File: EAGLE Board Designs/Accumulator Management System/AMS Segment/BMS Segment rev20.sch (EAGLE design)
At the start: 161 parts, among them J1 CONNECTOR-2_MICROFIT_SMD_RIGH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, J10 CONNECTOR-2_MICROFIT_SMD_RIGH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, J100 CONNECTOR-1_5222_, J101 CONNECTOR-1_5222_, J102 CONNECTOR-1_5222_, J103 CONNECTOR-1_5222_, J104 CONNECTOR-1_5222_, J105 CONNECTOR-1_5222_, J106 CONNECTOR-1_5222_, J107 CONNECTOR-1_5222_, J108 CONNECTOR-1_5222_, J109 CONNECTOR-1_5222_, J11 CONNECTOR-2_MICROFIT_SMD_RIGH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, J110 CONNECTOR-1_5222_, J111 CONNECTOR-1_5222_, J112 CONNECTOR-1_5222_, J113 CONNECTOR-1_5222_, J114 CONNECTOR-1_5222_, J115 CONNECTOR-1_5222_, J116 CONNECTOR-1_5222_, J117 CONNECTOR-1_5222_, J118 CONNECTOR-1_5222_, J119 CONNECTOR-1_5222_, J12 CONNECTOR-2_MICROFIT_SMD_RIGH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, J120 CONNECTOR-1_5222_, J121 CONNECTOR-1_5222_, J2 CONNECTOR-2_MICROFIT_SMD_RIGH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, J3 CONNECTOR-2_MICROFIT_SMD_RIGH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, J4 CONNECTOR-2_MICROFIT_SMD_RIGH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, J6 CONNECTOR-2_MICROFIT_SMD_RIGH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, J8 CONNECTOR-2_MICROFIT_SMD_RIGH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, J9 CONNECTOR-2_MICROFIT_SMD_RIGH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, T2 TRANSFORMER_HM2112ZNLT, U1 SHT31-ARP-B, U2 LTC6811-1, U3 LT3990-5, U4 LT3990-5, U5 LTC6811-1, U6 SHT31-ARP-B

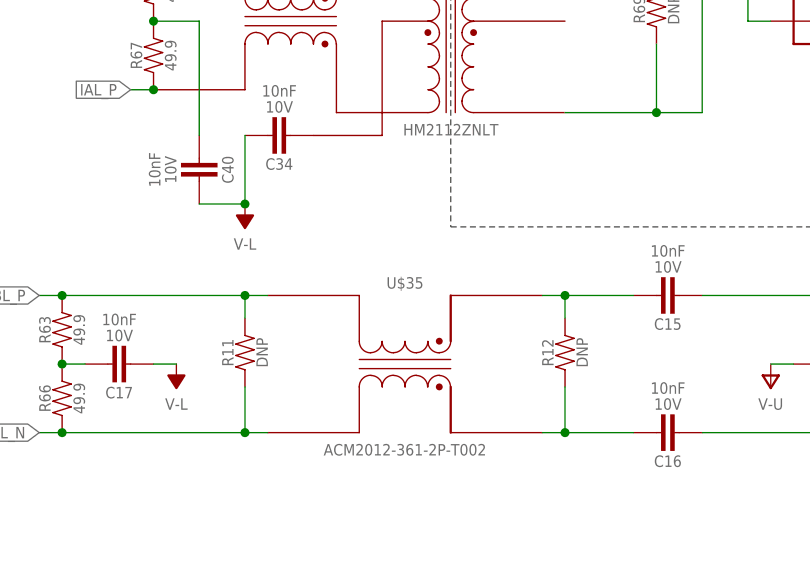
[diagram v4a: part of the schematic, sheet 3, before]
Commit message: Updates to Board
Added updates to board design.
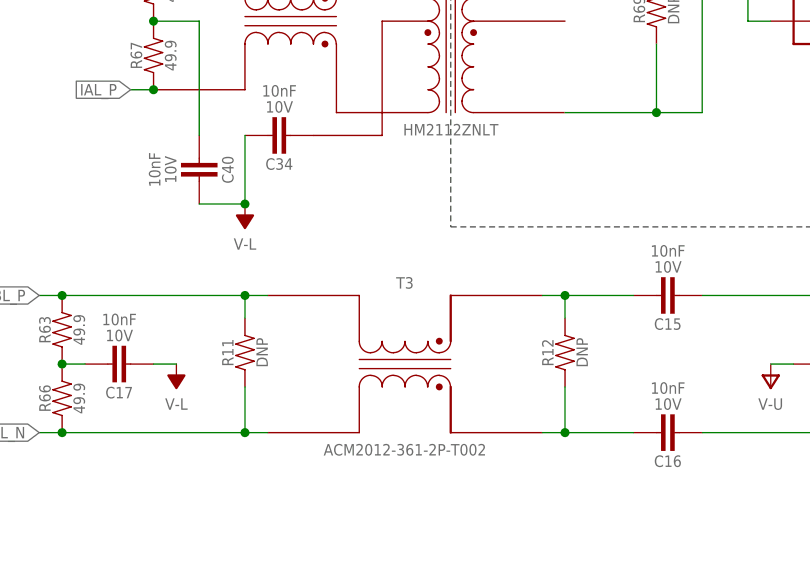
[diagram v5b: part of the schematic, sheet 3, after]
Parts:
- renumbered U$35 to T3
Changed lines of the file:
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@@
 <part name="P100" library="HyTechSupplies" deviceset="V-U" device=""/>
 <part name="R69" library="HyTechDevices" deviceset="RESISTOR_?_*" device="0603" technology="DNP" value="RESISTOR_0603_DNP"/>
-<part name="U$35" library="HyTechDevices" deviceset="ACM2012-361-2P-T002" device=""/>
+<part name="T3" library="HyTechDevices" deviceset="ACM2012-361-2P-T002" device=""/>
 <part name="U5" library="HyTechDevices" deviceset="LTC6811-1" device=""/>
 <part name="U2" library="HyTechDevices" deviceset="LTC6811-1" device=""/>
@@
 <attribute name="RESISTANCE" x="128.27" y="118.11" size="1.27" layer="96" rot="R90" align="top-center"/>
 </instance>
-<instance part="U$35" gate="G$1" x="99.06" y="78.74" smashed="yes">
+<instance part="T3" gate="G$1" x="99.06" y="78.74" smashed="yes">
 <attribute name="NAME" x="99.06" y="87.122" size="1.27" layer="95" align="bottom-center"/>
 <attribute name="MPN" x="99.06" y="69.85" size="1.27" layer="96" align="top-center"/>
@@
 <label x="58.42" y="71.12" size="1.27" layer="95" rot="R180" xref="yes"/>
 <pinref part="R66" gate="G$1" pin="1"/>
-<pinref part="U$35" gate="G$1" pin="2"/>
+<pinref part="T3" gate="G$1" pin="2"/>
 <wire x1="83.82" y1="71.12" x2="81.28" y2="71.12" width="0.1524" layer="91"/>
 <junction x="60.96" y="71.12"/>
@@
 <label x="58.42" y="86.36" size="1.27" layer="95" rot="R180" xref="yes"/>
 <pinref part="R63" gate="G$1" pin="2"/>
-<pinref part="U$35" gate="G$1" pin="1"/>
+<pinref part="T3" gate="G$1" pin="1"/>
 <wire x1="83.82" y1="86.36" x2="81.28" y2="86.36" width="0.1524" layer="91"/>
 <junction x="60.96" y="86.36"/>
@@
 <wire x1="124.46" y1="86.36" x2="116.84" y2="86.36" width="0.1524" layer="91"/>
 <wire x1="116.84" y1="86.36" x2="116.84" y2="83.82" width="0.1524" layer="91"/>
-<pinref part="U$35" gate="G$1" pin="4"/>
+<pinref part="T3" gate="G$1" pin="4"/>
 <wire x1="116.84" y1="86.36" x2="114.3" y2="86.36" width="0.1524" layer="91"/>
 <junction x="116.84" y="86.36"/>
@@
 <wire x1="124.46" y1="71.12" x2="116.84" y2="71.12" width="0.1524" layer="91"/>
 <wire x1="116.84" y1="71.12" x2="116.84" y2="76.2" width="0.1524" layer="91"/>
-<pinref part="U$35" gate="G$1" pin="3"/>
+<pinref part="T3" gate="G$1" pin="3"/>
 <wire x1="116.84" y1="71.12" x2="114.3" y2="71.12" width="0.1524" layer="91"/>
 <junction x="116.84" y="71.12"/>

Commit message: Added New Fuse Component
Changed fuses to cheaper, smaller package fuse components -- handles 3A, 125VDC.
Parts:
- F1, F10, F11, F12, F13, F14, F15, F16, F17, F18, F19, F2, F20, F21, F22, F23, F3, F4, F5, F6, F7, F8, F9: value FUSE_0885_1 -> FUSE__; device HyTechDevices:FUSE_0885_1 -> HyTechDevices:FUSE__2-SMD_3A
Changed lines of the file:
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@@
 <part name="P-4" library="HyTechSupplies" deviceset="V-L" device=""/>
 <part name="P+1" library="HyTechSupplies" deviceset="V+U" device=""/>
-<part name="F1" library="HyTechDevices" deviceset="FUSE_?_*" device="0885" technology="1" value="FUSE_0885_1"/>
-<part name="F4" library="HyTechDevices" deviceset="FUSE_?_*" device="0885" technology="1" value="FUSE_0885_1"/>
-<part name="F2" library="HyTechDevices" deviceset="FUSE_?_*" device="0885" technology="1" value="FUSE_0885_1"/>
-<part name="F5" library="HyTechDevices" deviceset="FUSE_?_*" device="0885" technology="1" value="FUSE_0885_1"/>
-<part name="F3" library="HyTechDevices" deviceset="FUSE_?_*" device="0885" technology="1" value="FUSE_0885_1"/>
-<part name="F9" library="HyTechDevices" deviceset="FUSE_?_*" device="0885" technology="1" value="FUSE_0885_1"/>
-<part name="F6" library="HyTechDevices" deviceset="FUSE_?_*" device="0885" technology="1" value="FUSE_0885_1"/>
-<part name="F10" library="HyTechDevices" deviceset="FUSE_?_*" device="0885" technology="1" value="FUSE_0885_1"/>
-<part name="F7" library="HyTechDevices" deviceset="FUSE_?_*" device="0885" technology="1" value="FUSE_0885_1"/>
-<part name="F11" library="HyTechDevices" deviceset="FUSE_?_*" device="0885" technology="1" value="FUSE_0885_1"/>
-<part name="F8" library="HyTechDevices" deviceset="FUSE_?_*" device="0885" technology="1" value="FUSE_0885_1"/>
-<part name="F13" library="HyTechDevices" deviceset="FUSE_?_*" device="0885" technology="1" value="FUSE_0885_1"/>
-<part name="F15" library="HyTechDevices" deviceset="FUSE_?_*" device="0885" technology="1" value="FUSE_0885_1"/>
-<part name="F14" library="HyTechDevices" deviceset="FUSE_?_*" device="0885" technology="1" value="FUSE_0885_1"/>
-<part name="F17" library="HyTechDevices" deviceset="FUSE_?_*" device="0885" technology="1" value="FUSE_0885_1"/>
-<part name="F16" library="HyTechDevices" deviceset="FUSE_?_*" device="0885" technology="1" value="FUSE_0885_1"/>
-<part name="F19" library="HyTechDevices" deviceset="FUSE_?_*" device="0885" technology="1" value="FUSE_0885_1"/>
-<part name="F18" library="HyTechDevices" deviceset="FUSE_?_*" device="0885" technology="1" value="FUSE_0885_1"/>
-<part name="F21" library="HyTechDevices" deviceset="FUSE_?_*" device="0885" technology="1" value="FUSE_0885_1"/>
+<part name="F1" library="HyTechDevices" deviceset="FUSE_?_*" device="" technology="2-SMD_3A" value="FUSE__"/>
+<part name="F4" library="HyTechDevices" deviceset="FUSE_?_*" device="" technology="2-SMD_3A" value="FUSE__"/>
+<part name="F2" library="HyTechDevices" deviceset="FUSE_?_*" device="" technology="2-SMD_3A" value="FUSE__"/>
+<part name="F5" library="HyTechDevices" deviceset="FUSE_?_*" device="" technology="2-SMD_3A" value="FUSE__"/>
+<part name="F3" library="HyTechDevices" deviceset="FUSE_?_*" device="" technology="2-SMD_3A" value="FUSE__"/>
+<part name="F9" library="HyTechDevices" deviceset="FUSE_?_*" device="" technology="2-SMD_3A" value="FUSE__"/>
+<part name="F6" library="HyTechDevices" deviceset="FUSE_?_*" device="" technology="2-SMD_3A" value="FUSE__"/>
+<part name="F10" library="HyTechDevices" deviceset="FUSE_?_*" device="" technology="2-SMD_3A" value="FUSE__"/>
+<part name="F7" library="HyTechDevices" deviceset="FUSE_?_*" device="" technology="2-SMD_3A" value="FUSE__"/>
+<part name="F11" library="HyTechDevices" deviceset="FUSE_?_*" device="" technology="2-SMD_3A" value="FUSE__"/>
+<part name="F8" library="HyTechDevices" deviceset="FUSE_?_*" device="" technology="2-SMD_3A" value="FUSE__"/>
+<part name="F13" library="HyTechDevices" deviceset="FUSE_?_*" device="" technology="2-SMD_3A" value="FUSE__"/>
+<part name="F15" library="HyTechDevices" deviceset="FUSE_?_*" device="" technology="2-SMD_3A" value="FUSE__"/>
+<part name="F14" library="HyTechDevices" deviceset="FUSE_?_*" device="" technology="2-SMD_3A" value="FUSE__"/>
+<part name="F17" library="HyTechDevices" deviceset="FUSE_?_*" device="" technology="2-SMD_3A" value="FUSE__"/>
+<part name="F16" library="HyTechDevices" deviceset="FUSE_?_*" device="" technology="2-SMD_3A" value="FUSE__"/>
+<part name="F19" library="HyTechDevices" deviceset="FUSE_?_*" device="" technology="2-SMD_3A" value="FUSE__"/>
+<part name="F18" library="HyTechDevices" deviceset="FUSE_?_*" device="" technology="2-SMD_3A" value="FUSE__"/>
+<part name="F21" library="HyTechDevices" deviceset="FUSE_?_*" device="" technology="2-SMD_3A" value="FUSE__"/>
 <part name="J101" library="HyTechDevices" deviceset="CONNECTOR-1_?_*" device="5222"/>
 <part name="J100" library="HyTechDevices" deviceset="CONNECTOR-1_?_*" device="5222"/>
@@
 <part name="J120" library="HyTechDevices" deviceset="CONNECTOR-1_?_*" device="5222"/>
 <part name="J121" library="HyTechDevices" deviceset="CONNECTOR-1_?_*" device="5222"/>
-<part name="F20" library="HyTechDevices" deviceset="FUSE_?_*" device="0885" technology="1" value="FUSE_0885_1"/>
-<part name="F22" library="HyTechDevices" deviceset="FUSE_?_*" device="0885" technology="1" value="FUSE_0885_1"/>
-<part name="F23" library="HyTechDevices" deviceset="FUSE_?_*" device="0885" technology="1" value="FUSE_0885_1"/>
+<part name="F20" library="HyTechDevices" deviceset="FUSE_?_*" device="" technology="2-SMD_3A" value="FUSE__"/>
+<part name="F22" library="HyTechDevices" deviceset="FUSE_?_*" device="" technology="2-SMD_3A" value="FUSE__"/>
+<part name="F23" library="HyTechDevices" deviceset="FUSE_?_*" device="" technology="2-SMD_3A" value="FUSE__"/>
 <part name="P26" library="HyTechSupplies" deviceset="V-U" device=""/>
 <part name="P28" library="HyTechSupplies" deviceset="V-U" device=""/>
@@
 <part name="P65" library="HyTechSupplies" deviceset="VREGU" device=""/>
 <part name="P66" library="HyTechSupplies" deviceset="VREGU" device=""/>
-<part name="F12" library="HyTechDevices" deviceset="FUSE_?_*" device="0885" technology="1" value="FUSE_0885_1"/>
+<part name="F12" library="HyTechDevices" deviceset="FUSE_?_*" device="" technology="2-SMD_3A" value="FUSE__"/>
 <part name="TP9" library="HyTechDevices" deviceset="TEST_POINT" device=""/>
 <part name="TP8" library="HyTechDevices" deviceset="TEST_POINT" device=""/>

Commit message: BMS Segment Universal Fuse, Buck
Fixed Buck routing and changed fuse footprint to universal footprint.
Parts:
- F1, F10, F11, F12, F13, F14, F15, F16, F17, F18, F19, F2, F20, F21, F22, F23, F3, F4, F5, F6, F7, F8, F9: device HyTechDevices:FUSE__2-SMD_3A -> HyTechDevices:FUSE_BMS-UNIVERSAL_
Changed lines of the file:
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@@
 <part name="P-4" library="HyTechSupplies" deviceset="V-L" device=""/>
 <part name="P+1" library="HyTechSupplies" deviceset="V+U" device=""/>
-<part name="F1" library="HyTechDevices" deviceset="FUSE_?_*" device="" technology="2-SMD_3A" value="FUSE__"/>
-<part name="F4" library="HyTechDevices" deviceset="FUSE_?_*" device="" technology="2-SMD_3A" value="FUSE__"/>
-<part name="F2" library="HyTechDevices" deviceset="FUSE_?_*" device="" technology="2-SMD_3A" value="FUSE__"/>
-<part name="F5" library="HyTechDevices" deviceset="FUSE_?_*" device="" technology="2-SMD_3A" value="FUSE__"/>
-<part name="F3" library="HyTechDevices" deviceset="FUSE_?_*" device="" technology="2-SMD_3A" value="FUSE__"/>
-<part name="F9" library="HyTechDevices" deviceset="FUSE_?_*" device="" technology="2-SMD_3A" value="FUSE__"/>
-<part name="F6" library="HyTechDevices" deviceset="FUSE_?_*" device="" technology="2-SMD_3A" value="FUSE__"/>
-<part name="F10" library="HyTechDevices" deviceset="FUSE_?_*" device="" technology="2-SMD_3A" value="FUSE__"/>
-<part name="F7" library="HyTechDevices" deviceset="FUSE_?_*" device="" technology="2-SMD_3A" value="FUSE__"/>
-<part name="F11" library="HyTechDevices" deviceset="FUSE_?_*" device="" technology="2-SMD_3A" value="FUSE__"/>
-<part name="F8" library="HyTechDevices" deviceset="FUSE_?_*" device="" technology="2-SMD_3A" value="FUSE__"/>
-<part name="F13" library="HyTechDevices" deviceset="FUSE_?_*" device="" technology="2-SMD_3A" value="FUSE__"/>
-<part name="F15" library="HyTechDevices" deviceset="FUSE_?_*" device="" technology="2-SMD_3A" value="FUSE__"/>
-<part name="F14" library="HyTechDevices" deviceset="FUSE_?_*" device="" technology="2-SMD_3A" value="FUSE__"/>
-<part name="F17" library="HyTechDevices" deviceset="FUSE_?_*" device="" technology="2-SMD_3A" value="FUSE__"/>
-<part name="F16" library="HyTechDevices" deviceset="FUSE_?_*" device="" technology="2-SMD_3A" value="FUSE__"/>
-<part name="F19" library="HyTechDevices" deviceset="FUSE_?_*" device="" technology="2-SMD_3A" value="FUSE__"/>
-<part name="F18" library="HyTechDevices" deviceset="FUSE_?_*" device="" technology="2-SMD_3A" value="FUSE__"/>
-<part name="F21" library="HyTechDevices" deviceset="FUSE_?_*" device="" technology="2-SMD_3A" value="FUSE__"/>
+<part name="F1" library="HyTechDevices" deviceset="FUSE_?_*" device="BMS-UNIVERSAL" value="FUSE__"/>
+<part name="F4" library="HyTechDevices" deviceset="FUSE_?_*" device="BMS-UNIVERSAL" value="FUSE__"/>
+<part name="F2" library="HyTechDevices" deviceset="FUSE_?_*" device="BMS-UNIVERSAL" value="FUSE__"/>
+<part name="F5" library="HyTechDevices" deviceset="FUSE_?_*" device="BMS-UNIVERSAL" value="FUSE__"/>
+<part name="F3" library="HyTechDevices" deviceset="FUSE_?_*" device="BMS-UNIVERSAL" value="FUSE__"/>
+<part name="F9" library="HyTechDevices" deviceset="FUSE_?_*" device="BMS-UNIVERSAL" value="FUSE__"/>
+<part name="F6" library="HyTechDevices" deviceset="FUSE_?_*" device="BMS-UNIVERSAL" value="FUSE__"/>
+<part name="F10" library="HyTechDevices" deviceset="FUSE_?_*" device="BMS-UNIVERSAL" value="FUSE__"/>
+<part name="F7" library="HyTechDevices" deviceset="FUSE_?_*" device="BMS-UNIVERSAL" value="FUSE__"/>
+<part name="F11" library="HyTechDevices" deviceset="FUSE_?_*" device="BMS-UNIVERSAL" value="FUSE__"/>
+<part name="F8" library="HyTechDevices" deviceset="FUSE_?_*" device="BMS-UNIVERSAL" value="FUSE__"/>
+<part name="F13" library="HyTechDevices" deviceset="FUSE_?_*" device="BMS-UNIVERSAL" value="FUSE__"/>
+<part name="F15" library="HyTechDevices" deviceset="FUSE_?_*" device="BMS-UNIVERSAL" value="FUSE__"/>
+<part name="F14" library="HyTechDevices" deviceset="FUSE_?_*" device="BMS-UNIVERSAL" value="FUSE__"/>
+<part name="F17" library="HyTechDevices" deviceset="FUSE_?_*" device="BMS-UNIVERSAL" value="FUSE__"/>
+<part name="F16" library="HyTechDevices" deviceset="FUSE_?_*" device="BMS-UNIVERSAL" value="FUSE__"/>
+<part name="F19" library="HyTechDevices" deviceset="FUSE_?_*" device="BMS-UNIVERSAL" value="FUSE__"/>
+<part name="F18" library="HyTechDevices" deviceset="FUSE_?_*" device="BMS-UNIVERSAL" value="FUSE__"/>
+<part name="F21" library="HyTechDevices" deviceset="FUSE_?_*" device="BMS-UNIVERSAL" value="FUSE__"/>
 <part name="J101" library="HyTechDevices" deviceset="CONNECTOR-1_?_*" device="5222"/>
 <part name="J100" library="HyTechDevices" deviceset="CONNECTOR-1_?_*" device="5222"/>
@@
 <part name="J120" library="HyTechDevices" deviceset="CONNECTOR-1_?_*" device="5222"/>
 <part name="J121" library="HyTechDevices" deviceset="CONNECTOR-1_?_*" device="5222"/>
-<part name="F20" library="HyTechDevices" deviceset="FUSE_?_*" device="" technology="2-SMD_3A" value="FUSE__"/>
-<part name="F22" library="HyTechDevices" deviceset="FUSE_?_*" device="" technology="2-SMD_3A" value="FUSE__"/>
-<part name="F23" library="HyTechDevices" deviceset="FUSE_?_*" device="" technology="2-SMD_3A" value="FUSE__"/>
+<part name="F20" library="HyTechDevices" deviceset="FUSE_?_*" device="BMS-UNIVERSAL" value="FUSE__"/>
+<part name="F22" library="HyTechDevices" deviceset="FUSE_?_*" device="BMS-UNIVERSAL" value="FUSE__"/>
+<part name="F23" library="HyTechDevices" deviceset="FUSE_?_*" device="BMS-UNIVERSAL" value="FUSE__"/>
 <part name="P26" library="HyTechSupplies" deviceset="V-U" device=""/>
 <part name="P28" library="HyTechSupplies" deviceset="V-U" device=""/>
@@
 <part name="P65" library="HyTechSupplies" deviceset="VREGU" device=""/>
 <part name="P66" library="HyTechSupplies" deviceset="VREGU" device=""/>
-<part name="F12" library="HyTechDevices" deviceset="FUSE_?_*" device="" technology="2-SMD_3A" value="FUSE__"/>
+<part name="F12" library="HyTechDevices" deviceset="FUSE_?_*" device="BMS-UNIVERSAL" value="FUSE__"/>
 <part name="TP9" library="HyTechDevices" deviceset="TEST_POINT" device=""/>
 <part name="TP8" library="HyTechDevices" deviceset="TEST_POINT" device=""/>

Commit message: New Temperature Measurement
Added new board temperature measurement IC.
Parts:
- removed C30: CAPACITOR_0603_10V_0.1UF, HyTechDevices:CAPACITOR_0603_10V_0.1UF
- removed C31: CAPACITOR_0603_10V_3.3NF, HyTechDevices:CAPACITOR_0603_10V_3.3NF
- removed R48: RESISTOR_0603_DNP, HyTechDevices:RESISTOR_0603_DNP
- removed R49: RESISTOR_0603_100, HyTechDevices:RESISTOR_0603_100
- removed U1, U6: SHT31-ARP-B, HyTechDevices:SHT31-ARP-B
- added R18, R19: RESISTOR_0603_210, HyTechDevices:RESISTOR_0603_210
- added R23, R24: RESISTOR_0603_DNP, HyTechDevices:RESISTOR_0603_DNP
- added U$35, U$36: MCP9701T-E/LT, HyTechDevices:MCP9701T-E/LT
- C1: value CAPACITOR_0603_10V_0.1UF -> CAPACITOR_0603_10V_1UF; device HyTechDevices:CAPACITOR_0603_10V_0.1UF -> HyTechDevices:CAPACITOR_0603_10V_1UF
- C2: value CAPACITOR_0603_10V_3.3NF -> CAPACITOR_0603_10V_1UF; device HyTechDevices:CAPACITOR_0603_10V_3.3NF -> HyTechDevices:CAPACITOR_0603_10V_1UF
- R1: value RESISTOR_0603_100 -> RESISTOR_0603_0; device HyTechDevices:RESISTOR_0603_100 -> HyTechDevices:RESISTOR_0603_0
- R2: value RESISTOR_0603_DNP -> RESISTOR_0603_0; device HyTechDevices:RESISTOR_0603_DNP -> HyTechDevices:RESISTOR_0603_0
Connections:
- removed net N$30: R49.1, U6.T
- removed net N$81: R1.2, U1.RH
- removed net N$83: R2.2, U1.T
- new net N$14: C2.1, R19.1, U$36.VDD
- new net TOUTL: R2.2, R24.2, U$36.VOUT
- new net TOUTU: R1.2, R23.2, U$35.VOUT
- net GPIO5L: no longer C2.1, R1.1
- net GPIO5U: now also R1.1; no longer C31.1, R48.1, R49.2
- net N$12: now also C1.1, R18.1, U$35.VDD; no longer R48.2, U6.RH
- net V-L: now also R24.1, U$36.GND; no longer C1.1, U1.GND
- net V-U: now also C1.2, R23.1, U$35.GND; no longer C30.2, C31.2, U6.GND
- net VREGL: now also R19.2; no longer C1.2, U1.VDD
- net VREGU: now also R18.2; no longer C30.1, U6.VDD
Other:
- note added: "Approximate 0.005 degree Celcius resolution from -10 to 125 degrees Celcius"
- note added: "Change value of resistor in series and capacitor in shunt if necessary (used 3.3nF capacitor in shunt and 100 Ohm resistor in series in the past)."
- moved on the sheet: C1, C2, C21, C22, C25, L2, R1, R2, R40, R41, U4
